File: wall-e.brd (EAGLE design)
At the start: 100 x 80 mm, 62 parts, among them IC1 VREG-TS1117CW-3V3, T1 BC847, U1 TSM2306CX, U2 TSM2306CX, U3 TSM2306CX, U4 TSM2306CX, U5 TSM2306CX, U6 TSM2306CX, U7 TSM2306CX, U8 LM293AD, U9 TSM2306CX

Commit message: Correction of the board
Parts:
- removed CODEUSE: (no value), con-amp:SMDTOP4
- removed D8: (no value), diode:SOD523
- removed R1: (no value), rcl:R0805
- added C14: 10nF, rcl:C0805
- added LED1: (no value), led:CHIP-LED0805
- added R19: 10k, rcl:R0805
- added R20: 2.2K, resistor:R0805
- added SV2, SV3: (no value), con-lstb:MA05-1
- added SV4, SV5: (no value), con-lstb:MA03-1
- added X2, X3: (no value), con-amp:SMDTOP4
- C1, C2: value (none) -> 10uF; device rcl:C1206 -> rcl:C0805
- C3: value (none) -> 1uF
- R17: value 220R -> 2.2K
- R6, R7: value 470 -> 10k
- R8: value 348R -> 360R
- moved C8 156.1 mm to (-68.6, 73.7)
- moved C7 155.5 mm to (-87.6, 64.8)
- moved C5 144.8 mm to (-74.9, 64.8)
- moved C6 132.9 mm to (-81.3, 64.8)
- moved C13 128.6 mm to (-30.5, 73.7)
- moved C4 123.2 mm to (-68.6, 64.8)
- moved U$1 68.8 mm to (-19.1, 47.0)
- moved R10 62.4 mm to (-16.5, 80.0)
- moved U4 58.3 mm to (-85.1, 24.1)
- moved C2 49.0 mm to (-62.2, 73.7)
- moved U7 39.8 mm to (-66.0, 35.6)
- moved U9 39.8 mm to (-85.1, 35.6)
- moved AX12 38.1 mm to (-31.8, 47.0)
- moved R5 29.7 mm to (-62.2, 64.8)
- moved R13 29.2 mm to (-24.1, 73.7)
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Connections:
- removed net AX12_RX: D8.A, R17.1
- removed net AX12_TX: R18.2, T1.3
- removed net BUTTON4: TOIT.7, U$1.41
- removed net CODEUSE1_TIM1: CODEUSE.1, U$1.16
- removed net CODEUSE1_TIM2: CODEUSE.2, U$1.17
- removed net CODEUSE2_TIM1: CODEUSE.3, U$1.27
- removed net CODEUSE2_TIM2: CODEUSE.4, U$1.28
- removed net N$11: R1.2, U$1.44
- removed net N$22: D9.C, R16.1, R17.2
- removed net N$29: D8.C, R18.1
- removed net SWDCLK: U$3.P$4
- removed net VCC: U8.8
- new net CODEUSE1: U$1.17, X2.3
- new net CODEUSE1_TIM: U$1.16, X2.2
- new net CODEUSE2: U$1.14, X3.3
- new net CODEUSE2_TIM: U$1.13, X3.2
- new net DEBUG_LED: LED1.A, U$1.2
- new net EYE1: SV4.1, U$1.27
- new net EYE2: SV5.1, U$1.28
- net +3V3: now also C14.2, C3.2, R17.1, R18.1, R19.2, SV1.1, SV1.2, U$3.P$1, U8.8
- net +5V: now also R20.1, SV3.5, SV4.2, SV5.2, X2.1, X3.1; no longer SV1.1
- net AX12-RX: now also D9.C, R16.1, U$1.30; no longer U$1.31
- net AX12-TX: now also R18.2, T1.3, U$1.31; no longer U$1.30
- net GND: now also C14.1, C3.1, LED1.C, SV3.3, SV3.4, SV4.3, SV5.3, U$1.44, U$3.P$3, U$3.P$5, U$3.P$9, X2.4, X3.4; no longer C3.2, R1.1
- net MCU_RESET: now also R19.1, TOIT.7, U$3.P$10; no longer C3.1
- net MOTOR1_PWM: now also SV2.2
- net MOTOR1_PWM_N: now also SV2.4
- net MOTOR2_PWM: now also SV2.3
- net MOTOR2_PWM_N: now also SV2.5
- net N$23: now also R20.2
- net N$25: now also R17.2
- net PUMP: now also U$1.25; no longer U$1.29
- net SENSOR1: now also U$1.26; no longer U$1.25
- net SENSOR2: now also U$1.29; no longer U$1.26
- net SWCLK: now also U$3.P$4
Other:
- board size 100 x 80 mm -> 160 x 100 mm

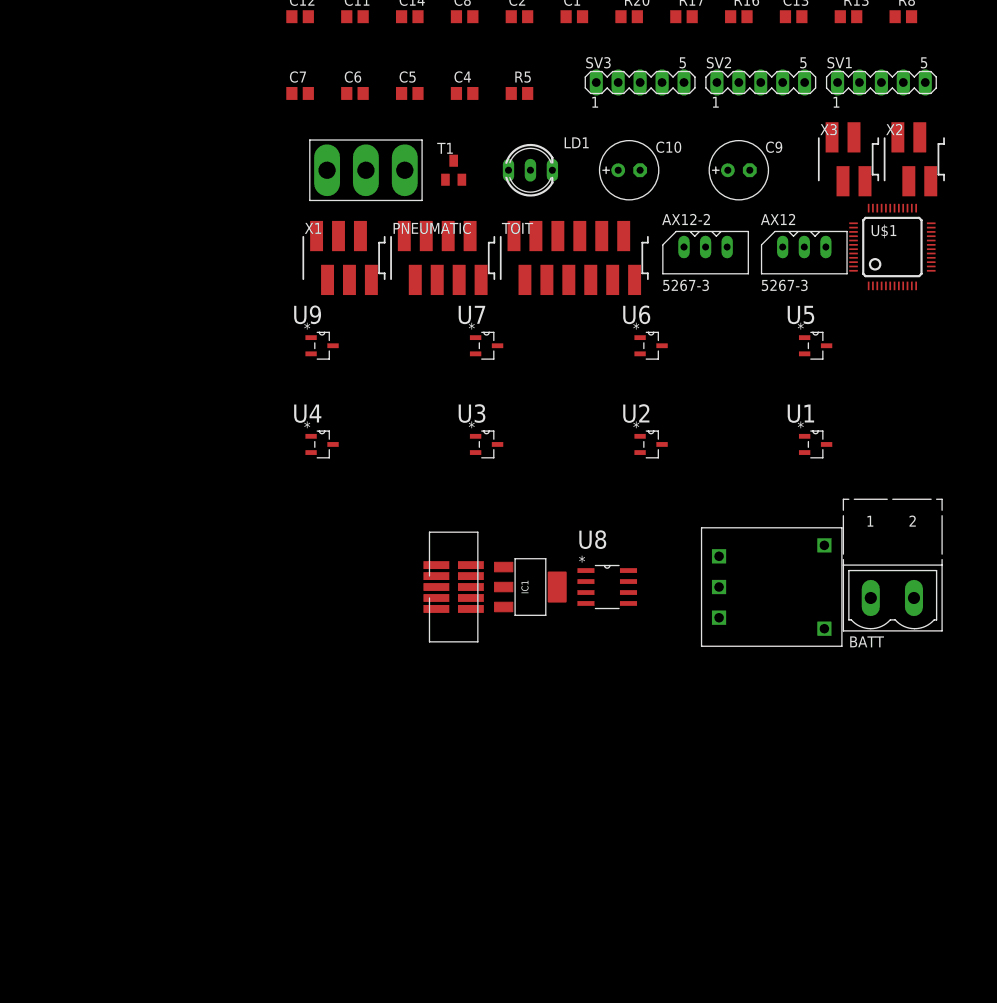
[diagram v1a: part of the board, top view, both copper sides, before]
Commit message: Change in the H bridge
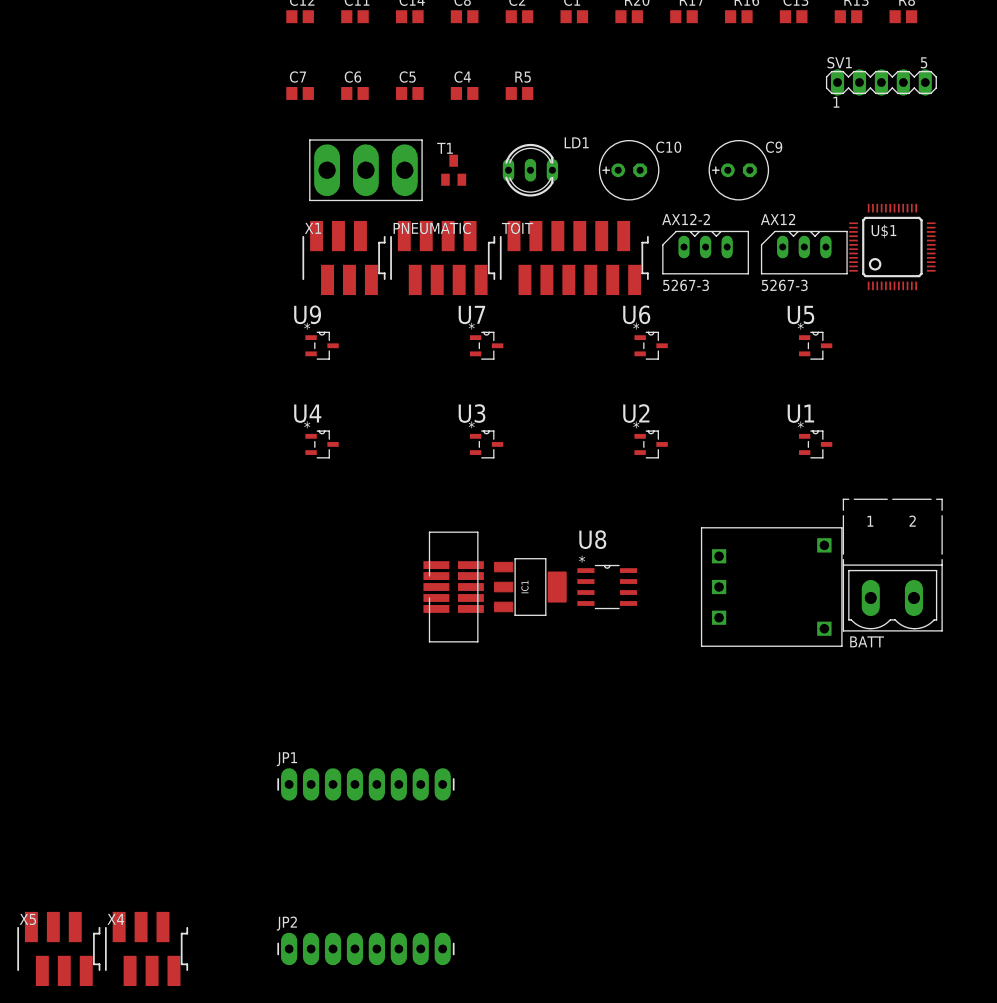
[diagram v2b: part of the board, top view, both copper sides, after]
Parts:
- removed SV2, SV3: (no value), con-lstb:MA05-1
- removed X2, X3: (no value), con-amp:SMDTOP4
- added JP1, JP2: (no value), SparkFun:1X08_LONGPADS
- added X4, X5: (no value), con-amp:SMDTOP6
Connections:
- new net MOTOR1_1: JP1.5, X4.4
- new net MOTOR1_2: JP1.4, X4.5
- new net MOTOR2_1: JP1.3, X5.4
- new net MOTOR2_2: JP1.2, X5.5
- net +12V: now also JP1.8
- net +3V3: now also JP1.7, JP2.1, JP2.4, JP2.7
- net +5V: now also X4.1, X5.1; no longer SV3.5, X2.1, X3.1
- net CODEUSE1: now also X4.3; no longer X2.3
- net CODEUSE1_TIM: now also X4.2; no longer X2.2
- net CODEUSE2: now also X5.3; no longer X3.3
- net CODEUSE2_TIM: now also X5.2; no longer X3.2
- net GND: now also JP1.1, JP1.6, JP2.8, X4.6, X5.6; no longer SV3.3, SV3.4, X2.4, X3.4
- net MOTOR1_PWM: now also JP2.3; no longer SV2.2
- net MOTOR1_PWM_N: now also JP2.2; no longer SV2.4
- net MOTOR2_PWM: now also JP2.5; no longer SV2.3
- net MOTOR2_PWM_N: now also JP2.6; no longer SV2.5

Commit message: Last corrections on the schematic
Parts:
- added C15: 100nF, rcl:C0805
- added R1: 2.2k, rcl:R0805
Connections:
- removed net DEBUG_LED: LED1.A, U$1.2
- new net N$11: R1.1, U$1.2
- new net N$18: LED1.A, R1.2
- net GND: now also C15.2
- net MCU_RESET: now also C15.1
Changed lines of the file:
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@@
 <element name="X4" library="con-amp" package="SMDTOP6" value="" x="-105.41" y="-34.29"/>
 <element name="X5" library="con-amp" package="SMDTOP6" value="" x="-115.57" y="-34.29"/>
+<element name="C15" library="rcl" package="C0805" value="100nF" x="-118.11" y="-46.99"/>
+<element name="R1" library="rcl" package="R0805" value="2.2k" x="-118.11" y="-53.34"/>
 </elements>
 <signals>
@@
 <contactref element="SV4" pad="3"/>
 <contactref element="SV5" pad="3"/>
-<contactref element="LED1" pad="C"/>
 <contactref element="JP1" pad="1"/>
 <contactref element="JP1" pad="6"/>
@@
 <contactref element="X4" pad="6"/>
 <contactref element="X5" pad="6"/>
+<contactref element="C15" pad="2"/>
+<contactref element="LED1" pad="C"/>
+<wire x1="-112.395" y1="-36.83" x2="-117.16" y2="-46.99" width="0" layer="19" extent="1-1"/>
 <wire x1="-102.235" y1="-36.83" x2="-112.395" y2="-36.83" width="0" layer="19" extent="1-1"/>
 <wire x1="-88.9" y1="-15.24" x2="-102.235" y2="-36.83" width="0" layer="19" extent="1-1"/>
@@
 <contactref element="U$3" pad="P$10"/>
 <contactref element="TOIT" pad="7"/>
+<contactref element="C15" pad="1"/>
+<wire x1="-67.85" y1="5.08" x2="-119.06" y2="-46.99" width="0" layer="19" extent="1-1"/>
 <wire x1="-55.245" y1="48.26" x2="-67.85" y2="5.08" width="0" layer="19" extent="1-1"/>
 <wire x1="-55.56" y1="80.01" x2="-55.245" y2="48.26" width="0" layer="19" extent="1-1"/>
@@
 <wire x1="-14.55" y1="46.24" x2="-106.045" y2="-31.75" width="0" layer="19" extent="1-1"/>
 </signal>
-<signal name="DEBUG_LED">
-<contactref element="U$1" pad="2"/>
-<contactref element="LED1" pad="A"/>
-<wire x1="-21.3" y1="42.49" x2="-19.05" y2="84.04" width="0" layer="19" extent="1-1"/>
-</signal>
 <signal name="MOTOR1_1">
 <contactref element="JP1" pad="5"/>
@@
 <wire x1="-86.36" y1="-15.24" x2="-113.665" y2="-31.75" width="0" layer="19" extent="1-1"/>
 </signal>
+<signal name="N$11">
+<contactref element="U$1" pad="2"/>
+<contactref element="R1" pad="1"/>
+<wire x1="-21.3" y1="42.49" x2="-119.06" y2="-53.34" width="0" layer="19" extent="1-1"/>
+</signal>
+<signal name="N$18">
+<contactref element="R1" pad="2"/>
+<contactref element="LED1" pad="A"/>
+<wire x1="-19.05" y1="84.04" x2="-117.16" y2="-53.34" width="0" layer="19" extent="1-1"/>
+</signal>
 </signals>

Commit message: Placement of the decoupling capacitor
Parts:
- moved C7 168.0 mm to (80.0, 53.7), flipped to the bottom, turned to 180 degrees
- moved C6 160.6 mm to (78.4, 47.0), flipped to the bottom, turned to 90 degrees
- moved C5 159.7 mm to (83.5, 45.2), flipped to the bottom
- moved C8 158.6 mm to (88.5, 52.1), flipped to the bottom, turned to 270 degrees
- moved C4 155.5 mm to (86.4, 52.1), flipped to the bottom, turned to 270 degrees
- moved C13 109.9 mm to (76.2, 47.0), flipped to the bottom, turned to 90 degrees
- moved U$1 101.6 mm to (82.5, 49.5)

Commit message: Placement of main components
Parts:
- moved X5 234.3 mm to (108.7, 33.9), turned to 270 degrees
- moved X4 221.8 mm to (108.7, 23.6), turned to 270 degrees
- moved R1 218.3 mm to (78.4, 41.6), flipped to the bottom, turned to 270 degrees
- moved JP1 190.1 mm to (97.2, 23.2), turned to 90 degrees
- moved U9 188.9 mm to (103.7, 29.2)
- moved C11 186.9 mm to (102.2, 38.1), flipped to the bottom
- moved JP2 186.7 mm to (82.0, 41.0), turned to 270 degrees
- moved R7 182.0 mm to (90.0, 30.3), turned to 90 degrees
- moved U4 176.2 mm to (89.9, 44.8)
- moved T1 175.1 mm to (102.0, 22.2)
- moved R6 171.4 mm to (86.4, 38.6), turned to 90 degrees
- moved PNEUMATIC 168.8 mm to (97.2, 58.5)
- moved R18 168.7 mm to (104.7, 8.76)
- moved U3 167.4 mm to (99.8, 47.1)
- moved R9 166.5 mm to (102.0, 40.6)
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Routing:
- net GND: track 0.00 -> 37.4 mm, vias 0 -> 4
- net +3V3: track 0.00 -> 19.1 mm, vias 0 -> 5
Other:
- board size 160 x 100 mm -> 61.3 x 46.5 mm

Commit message: Placement
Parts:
- removed ON/OFF: SWITCH, switch:SWITCH
- added C16: 100nF, rcl:C0805
- moved C15 198.2 mm to (59.9, 40.0), flipped to the bottom, turned to 180 degrees
- moved C14 164.5 mm to (86.8, 44.0), flipped to the bottom, turned to 270 degrees
- moved D9 163.1 mm to (93.5, 40.8), turned to 270 degrees
- moved C12 158.5 mm to (66.9, 38.4), flipped to the bottom
- moved C2 156.2 mm to (91.1, 44.0), flipped to the bottom, turned to 90 degrees
- moved C1 153.0 mm to (91.1, 31.2), flipped to the bottom, turned to 180 degrees
- moved R19 122.3 mm to (60.0, 37.1), flipped to the bottom, turned to 180 degrees
- moved C3 110.6 mm to (86.8, 43.9), turned to 270 degrees
- moved R12 107.6 mm to (71.5, 42.0), flipped to the bottom, turned to 270 degrees
- moved R11 104.1 mm to (74.0, 42.0), flipped to the bottom, turned to 90 degrees
- moved R13 98.4 mm to (69.0, 42.0), flipped to the bottom, turned to 90 degrees
- moved R10 98.0 mm to (65.5, 26.4), flipped to the bottom
- moved R17 47.7 mm to (102.4, 38.1), flipped to the bottom, turned to 180 degrees
- moved R9 35.1 mm to (70.0, 26.3), flipped to the bottom
- moved R18 29.4 mm to (102.5, 38.1)
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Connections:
- removed net N$30: BATT.1, ON/OFF.P$3
- net +12V: now also BATT.1; no longer ON/OFF.P$1, ON/OFF.P$2
- net +3V3: no longer U8.8
- net +5V: now also C16.2, U8.8
- net GND: now also C16.1
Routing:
- net N$16: track 0.00 -> 16.5 mm, vias 0 -> 2
- net N$20: track 0.00 -> 12.9 mm
- net MCU_RESET: track 0.00 -> 9.88 mm, vias 0 -> 1
- net N$17: track 0.00 -> 9.15 mm
- net N$21: track 0.00 -> 8.27 mm
- net GND: track 37.4 -> 44.1 mm
- net N$19: track 0.00 -> 5.94 mm
- net N$13: track 0.00 -> 5.65 mm
- net N$25: track 0.00 -> 4.91 mm
- net N$15: track 0.00 -> 4.36 mm
- net N$1: track 0.00 -> 4.33 mm, vias 0 -> 1
- net N$4: track 0.00 -> 4.32 mm, vias 0 -> 1
- net N$3: track 0.00 -> 3.97 mm, vias 0 -> 1
- net AX12-TX: track 0.00 -> 3.70 mm, vias 0 -> 1
- net N$9: track 0.00 -> 3.64 mm
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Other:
- board size 61.3 x 46.5 mm -> 61.3 x 51.1 mm

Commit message: Better allocation of the pins
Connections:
- new net AX12_RX: U$1.46
- new net AX12_TX: U$1.45
- new net N$22: U$1.26
- net AX12-RX: no longer U$1.30
- net AX12-TX: no longer U$1.31
- net BUTTON1: now also U$1.10; no longer U$1.38
- net BUTTON2: now also U$1.11; no longer U$1.39
- net CODEUSE1: now also U$1.30; no longer U$1.17
- net CODEUSE1_TIM: now also U$1.29; no longer U$1.16
- net CODEUSE2: now also U$1.39; no longer U$1.14
- net CODEUSE2_TIM: now also U$1.38; no longer U$1.13
- net JACK: now also U$1.14; no longer U$1.10
- net LED3: now also U$1.16; no longer U$1.45
- net LED4: now also U$1.17; no longer U$1.46
- net MOTOR1_PWM: now also U$1.12; no longer U$1.11
- net MOTOR2_PWM: now also U$1.13; no longer U$1.12
- net SENSOR1: now also U$1.41; no longer U$1.26
- net SENSOR2: now also U$1.31; no longer U$1.29
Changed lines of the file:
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@@
 </signal>
 <signal name="JACK">
-<contactref element="U$1" pad="10"/>
 <contactref element="TOIT" pad="2"/>
-<wire x1="61.46" y1="37.925" x2="84.3" y2="45.03" width="0" layer="19" extent="1-1"/>
+<contactref element="U$1" pad="14"/>
+<wire x1="61.46" y1="37.925" x2="87.05" y2="47.28" width="0" layer="19" extent="1-1"/>
 </signal>
 <signal name="MOTOR1_PWM">
-<contactref element="U$1" pad="11"/>
 <contactref element="U6" pad="1"/>
 <contactref element="JP2" pad="3"/>
-<wire x1="82" y1="35.92" x2="84.8" y2="45.03" width="0" layer="19" extent="1-1"/>
+<contactref element="U$1" pad="12"/>
+<wire x1="82" y1="35.92" x2="85.3" y2="45.03" width="0" layer="19" extent="1-1"/>
 <wire x1="84.73" y1="34.3298" x2="82" y2="35.92" width="0" layer="19" extent="1-1"/>
 </signal>
@@
 </signal>
 <signal name="BUTTON1">
-<contactref element="U$1" pad="38"/>
 <contactref element="TOIT" pad="4"/>
-<wire x1="61.46" y1="40.465" x2="78.05" y2="51.78" width="0" layer="19" extent="1-1"/>
+<contactref element="U$1" pad="10"/>
+<wire x1="61.46" y1="40.465" x2="84.3" y2="45.03" width="0" layer="19" extent="1-1"/>
 </signal>
 <signal name="BUTTON2">
-<contactref element="U$1" pad="39"/>
 <contactref element="TOIT" pad="5"/>
-<wire x1="56.38" y1="41.735" x2="78.05" y2="51.28" width="0" layer="19" extent="1-1"/>
+<contactref element="U$1" pad="11"/>
+<wire x1="56.38" y1="41.735" x2="84.8" y2="45.03" width="0" layer="19" extent="1-1"/>
 </signal>
 <signal name="BUTTON3">
@@
 </signal>
 <signal name="LED3">
-<contactref element="U$1" pad="45"/>
 <contactref element="R3" pad="1"/>
-<wire x1="63.24" y1="49.69" x2="78.05" y2="48.28" width="0" layer="19" extent="1-16"/>
+<contactref element="U$1" pad="16"/>
+<wire x1="63.24" y1="49.69" x2="87.05" y2="48.28" width="0" layer="19" extent="1-16"/>
 </signal>
 <signal name="LED4">
-<contactref element="U$1" pad="46"/>
 <contactref element="R5" pad="1"/>
-<wire x1="60.72" y1="51.24" x2="78.05" y2="47.78" width="0" layer="19" extent="1-16"/>
+<contactref element="U$1" pad="17"/>
+<wire x1="60.72" y1="51.24" x2="87.05" y2="48.78" width="0" layer="19" extent="1-16"/>
 </signal>
 <signal name="N$8">
@@
 <contactref element="R16" pad="1"/>
 <contactref element="D9" pad="C"/>
-<contactref element="U$1" pad="30"/>
-<wire x1="93.5" y1="41.4" x2="82.8" y2="54.03" width="0" layer="19" extent="1-1"/>
 <wire x1="101.19" y1="29.23" x2="93.5" y2="41.4" width="0" layer="19" extent="1-1"/>
 </signal>
@@
 <contactref element="T1" pad="3"/>
 <contactref element="R18" pad="2"/>
-<contactref element="U$1" pad="31"/>
 <wire x1="103.39" y1="34.41" x2="103.41" y2="34.41" width="0.4064" layer="16"/>
 <wire x1="103.41" y1="34.41" x2="103.41" y2="35.45" width="0.4064" layer="16"/>
@@
 <wire x1="103.41" y1="35.45" x2="103.4" y2="35.45" width="0.4064" layer="1"/>
 <wire x1="103.4" y1="35.45" x2="103.4" y2="38.08" width="0.4064" layer="1"/>
-<wire x1="103.4" y1="38.08" x2="82.3" y2="54.03" width="0" layer="19" extent="1-1"/>
 </signal>
 <signal name="IMU_SCL">
@@
 <signal name="SENSOR1">
 <contactref element="X1" pad="2"/>
-<contactref element="U$1" pad="26"/>
-<wire x1="61.245" y1="61" x2="84.8" y2="54.03" width="0" layer="19" extent="1-1"/>
+<contactref element="U$1" pad="41"/>
+<wire x1="61.245" y1="61" x2="78.05" y2="50.28" width="0" layer="19" extent="1-1"/>
 </signal>
 <signal name="SENSOR2">
 <contactref element="X1" pad="3"/>
-<contactref element="U$1" pad="29"/>
-<wire x1="62.515" y1="66.08" x2="83.3" y2="54.03" width="0" layer="19" extent="1-1"/>
+<contactref element="U$1" pad="31"/>
+<wire x1="62.515" y1="66.08" x2="82.3" y2="54.03" width="0" layer="19" extent="1-1"/>
 </signal>
 <signal name="SENSOR3">
@@
 </signal>
 <signal name="MOTOR2_PWM">
-<contactref element="U$1" pad="12"/>
 <contactref element="U7" pad="1"/>
 <contactref element="JP2" pad="5"/>
-<wire x1="82" y1="30.84" x2="85.3" y2="45.03" width="0" layer="19" extent="1-1"/>
+<contactref element="U$1" pad="13"/>
+<wire x1="82" y1="30.84" x2="87.05" y2="46.78" width="0" layer="19" extent="1-1"/>
 <wire x1="85.23" y1="29.2698" x2="82" y2="30.84" width="0" layer="19" extent="1-1"/>
 </signal>
@@
 </signal>
 <signal name="CODEUSE2_TIM">
-<contactref element="U$1" pad="13"/>
 <contactref element="X5" pad="2"/>
-<wire x1="87.05" y1="46.78" x2="107.28" y2="37.025" width="0" layer="19" extent="1-1"/>
+<contactref element="U$1" pad="38"/>
+<wire x1="78.05" y1="51.78" x2="107.28" y2="37.025" width="0" layer="19" extent="1-1"/>
 </signal>
 <signal name="CODEUSE2">
-<contactref element="U$1" pad="14"/>
 <contactref element="X5" pad="3"/>
-<wire x1="87.05" y1="47.28" x2="112.36" y2="35.755" width="0" layer="19" extent="1-1"/>
+<contactref element="U$1" pad="39"/>
+<wire x1="78.05" y1="51.28" x2="112.36" y2="35.755" width="0" layer="19" extent="1-1"/>
 </signal>
 <signal name="CODEUSE1_TIM">
-<contactref element="U$1" pad="16"/>
 <contactref element="X4" pad="2"/>
-<wire x1="107.25" y1="25.945" x2="87.05" y2="48.28" width="0" layer="19" extent="1-1"/>
+<contactref element="U$1" pad="29"/>
+<wire x1="107.25" y1="25.945" x2="83.3" y2="54.03" width="0" layer="19" extent="1-1"/>
 </signal>
 <signal name="CODEUSE1">
-<contactref element="U$1" pad="17"/>
 <contactref element="X4" pad="3"/>
-<wire x1="112.33" y1="24.675" x2="87.05" y2="48.78" width="0" layer="19" extent="1-1"/>
+<contactref element="U$1" pad="30"/>
+<wire x1="82.8" y1="54.03" x2="112.33" y2="24.675" width="0" layer="19" extent="1-1"/>
 </signal>
 <signal name="MOTOR1_1">
@@
 <wire x1="78.43" y1="40.43" x2="78.42" y2="40.69" width="0" layer="19" extent="1-16"/>
 </signal>
+<signal name="N$22">
+<contactref element="U$1" pad="26"/>
+</signal>
+<signal name="AX12_TX">
+<contactref element="U$1" pad="45"/>
+</signal>
+<signal name="AX12_RX">
+<contactref element="U$1" pad="46"/>
+</signal>
 </signals>

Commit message: Routing
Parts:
- moved R19 61.2 mm to (119.0, 53.4)
- moved C15 60.3 mm to (117.4, 58.3), turned to 270 degrees
- moved SV1 55.6 mm to (57.9, 46.6), turned to 90 degrees
- moved TOIT 52.8 mm to (109.6, 58.5)
- moved R2 47.5 mm to (105.3, 61.6), turned to 180 degrees
- moved R5 47.4 mm to (105.4, 64.3), turned to 180 degrees
- moved R4 47.1 mm to (105.3, 56.6), turned to 180 degrees
- moved R3 43.3 mm to (105.3, 59.1), turned to 180 degrees
- moved C14 6.53 mm to (83.3, 49.4)
- moved X4 2.19 mm to (108.2, 22.5), turned to 180 degrees
- moved X5 1.95 mm to (110.1, 33.2)
- moved AX12 1.88 mm to (106.2, 42.8)
- moved C3 1.61 mm to (88.5, 43.9), flipped to the bottom
- moved SV4 0.12 mm to (88.9, 63.0)
- moved SV5 0.08 mm to (84.6, 63.0)
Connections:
- net LED1: now also R5.1, U$1.22; no longer R4.1, U$1.21
- net LED2: now also R3.1, U$1.17; no longer R2.1, U$1.22
- net LED3: now also R4.1; no longer R3.1
- net LED4: now also R2.1, U$1.21; no longer R5.1, U$1.17
- net SENSOR3: now also X1.5; no longer X1.4
- net SENSOR4: now also X1.4; no longer X1.5
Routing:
- net GND: track 44.1 -> 95.7 mm, vias 4 -> 5
- net +5V: track 0.00 -> 45.0 mm, vias 0 -> 2
- net SENSOR2: track 0.00 -> 33.8 mm, vias 0 -> 2
- net SENSOR3: track 0.00 -> 30.5 mm, vias 0 -> 2
- net SENSOR1: track 0.00 -> 27.6 mm
- net SENSOR4: track 0.00 -> 25.3 mm, vias 0 -> 2
- net LED3: track 0.00 -> 25.0 mm, vias 0 -> 1
- net +3V3: track 19.1 -> 42.7 mm
- net LED1: track 0.00 -> 22.8 mm, vias 0 -> 1
- net LED4: track 0.00 -> 22.5 mm, vias 0 -> 1
- net LED2: track 0.00 -> 22.4 mm, vias 0 -> 1
- net IMU_SCL: track 0.00 -> 22.2 mm
- net IMU_SDA: track 0.00 -> 20.9 mm, vias 0 -> 1
- net AX12-RX: track 0.00 -> 20.9 mm
- net MCU_RESET: track 9.88 -> 28.9 mm, vias 1 -> 2
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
